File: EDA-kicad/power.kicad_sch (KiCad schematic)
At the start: 99 parts, among them SW6 CHP-041B, U10 BAT-CONNECTOR-FLTS22WR00, U11 BQ25792RQMR, U2 TPS650250RHBR, U3 MP3429GL-Z, U4 TPS650250RHBR

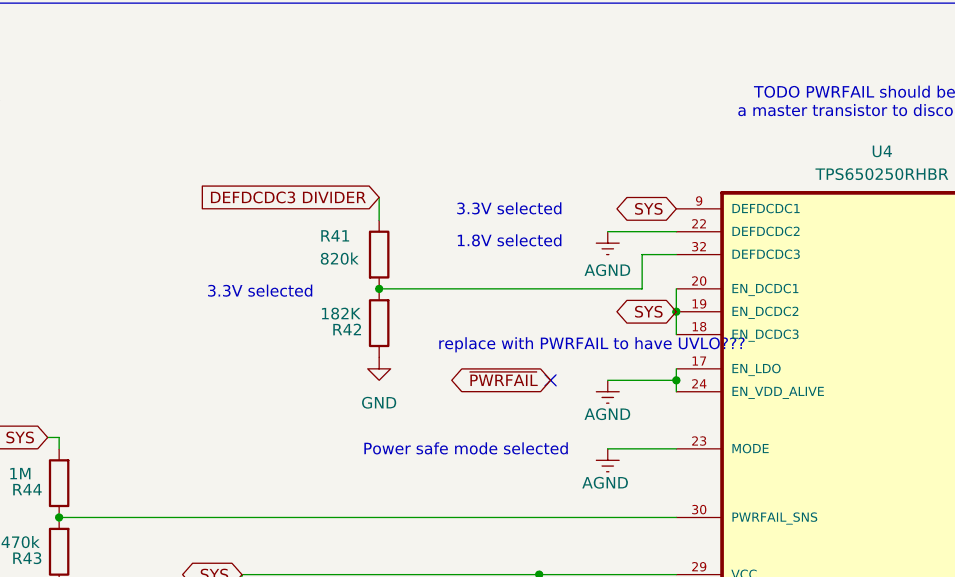
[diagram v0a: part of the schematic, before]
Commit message: separate regulator EN labels for fine grained power saving features etc
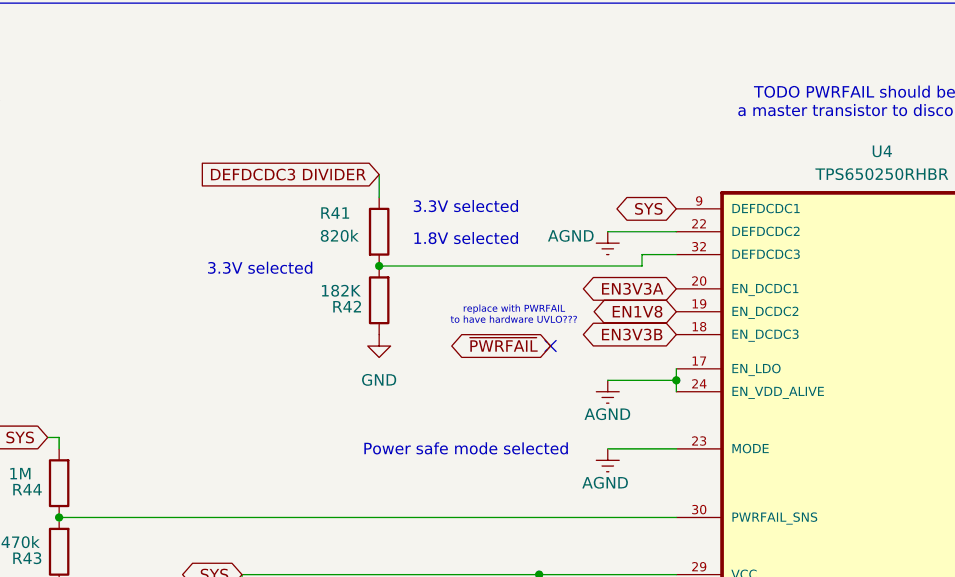
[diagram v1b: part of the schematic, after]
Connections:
- net SYS: no longer U4.18 (EN_DCDC3), U4.19 (EN_DCDC2), U4.20 (EN_DCDC1)
- new net EN1V8: U4.19 (EN_DCDC2)
- new net EN3V3A: U4.20 (EN_DCDC1)
- new net EN3V3B: U4.18 (EN_DCDC3)
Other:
- note added: "replace with PWRFAIL to have hardware UVLO???"
- note removed: "replace with PWRFAIL to have UVLO???"
- moved on the sheet: R41, R42
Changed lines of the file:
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@@
 	(text "1.8V selected"
 		(exclude_from_sim no)
-		(at 321.818 77.47 0)
+		(at 316.992 77.216 0)
 		(effects
 			(font
@@
 		)
 	)
-	(text "replace with PWRFAIL to have UVLO???\n"
+	(text "replace with PWRFAIL\nto have hardware UVLO???\n"
 		(exclude_from_sim no)
-		(at 330.962 88.9 0)
+		(at 322.326 85.598 0)
 		(effects
 			(font
-				(size 1.27 1.27)
+				(size 0.762 0.762)
 			)
 		)
@@
 	(text "3.3V selected"
 		(exclude_from_sim no)
-		(at 294.132 83.058 0)
+		(at 294.132 80.518 0)
 		(effects
 			(font
@@
 	(text "3.3V selected"
 		(exclude_from_sim no)
-		(at 321.818 73.914 0)
+		(at 316.992 73.66 0)
 		(effects
 			(font
@@
 	)
 	(junction
-		(at 307.34 82.55)
+		(at 307.34 80.01)
 		(diameter 0)
 		(color 0 0 0 0)
@@
 	)
 	(junction
-		(at 340.36 85.09)
-		(diameter 0)
-		(color 0 0 0 0)
-	)
-	(junction
 		(at 294.64 121.92)
 		(diameter 0)
@@
 	)
 	(no_connect
-		(at 326.39 92.71)
+		(at 326.39 88.9)
 	)
 	(no_connect
@@
 	(wire
 		(pts
-			(xy 340.36 82.55) (xy 340.36 85.09)
-		)
-		(stroke
-			(width 0)
-			(type default)
-		)
-	)
-	(wire
-		(pts
 			(xy 201.93 205.74) (xy 196.85 205.74)
 		)
@@
 	(wire
 		(pts
-			(xy 340.36 85.09) (xy 340.36 87.63)
-		)
-		(stroke
-			(width 0)
-			(type default)
-		)
-	)
-	(wire
-		(pts
 			(xy 52.07 227.33) (xy 57.15 227.33)
 		)
@@
 	(wire
 		(pts
-			(xy 307.34 82.55) (xy 336.55 82.55)
+			(xy 307.34 80.01) (xy 336.55 80.01)
 		)
 		(stroke
@@
 	(wire
 		(pts
-			(xy 336.55 78.74) (xy 336.55 82.55)
+			(xy 336.55 78.74) (xy 336.55 80.01)
 		)
 		(stroke
@@
 	(wire
 		(pts
-			(xy 307.34 72.39) (xy 307.34 74.93)
+			(xy 307.34 69.85) (xy 307.34 72.39)
 		)
 		(stroke
@@
 		)
 	)
+	(global_label "EN3V3B"
+		(shape bidirectional)
+		(at 340.36 87.63 180)
+		(fields_autoplaced yes)
+		(effects
+			(font
+				(size 1.27 1.27)
+			)
+			(justify right)
+		)
+		(property "Intersheetrefs" "${INTERSHEET_REFS}"
+			(at 329.0064 87.63 0)
+			(effects
+				(font
+					(size 1.27 1.27)
+				)
+				(justify right)
+				(hide yes)
+			)
+		)
+	)
 	(global_label "REGN"
 		(shape bidirectional)
@@
 		)
 	)
+	(global_label "EN1V8"
+		(shape bidirectional)
+		(at 340.36 85.09 180)
+		(fields_autoplaced yes)
+		(effects
+			(font
+				(size 1.27 1.27)
+			)
+			(justify right)
+		)
+		(property "Intersheetrefs" "${INTERSHEET_REFS}"
+			(at 330.2764 85.09 0)
+			(effects
+				(font
+					(size 1.27 1.27)
+				)
+				(justify right)
+				(hide yes)
+			)
+		)
+	)
 	(global_label "VDCDC1"
 		(shape input)
@@
 	(global_label "DEFDCDC3 DIVIDER"
 		(shape input)
-		(at 307.34 72.39 180)
+		(at 307.34 69.85 180)
 		(fields_autoplaced yes)
 		(effects
@@
 		)
 		(property "Intersheetrefs" "${INTERSHEET_REFS}"
-			(at 286.3329 72.39 0)
+			(at 286.3329 69.85 0)
 			(effects
 				(font
@@
 	(global_label "~{PWRFAIL}"
 		(shape bidirectional)
-		(at 326.39 92.71 180)
+		(at 326.39 88.9 180)
 		(fields_autoplaced yes)
 		(effects
@@
 		)
 		(property "Intersheetrefs" "${INTERSHEET_REFS}"
-			(at 314.492 92.71 0)
+			(at 314.492 88.9 0)
 			(effects
 				(font
@@
 		)
 	)
-	(global_label "SYS"
-		(shape bidirectional)
-		(at 340.36 85.09 180)
-		(fields_autoplaced yes)
-		(effects
-			(font
-				(size 1.27 1.27)
-			)
-			(justify right)
-		)
-		(property "Intersheetrefs" "${INTERSHEET_REFS}"
-			(at 332.7559 85.09 0)
-			(effects
-				(font
-					(size 1.27 1.27)
-				)
-				(justify right)
-				(hide yes)
-			)
-		)
-	)
 	(global_label "D+"
 		(shape bidirectional)
@@
 		)
 	)
+	(global_label "EN3V3A"
+		(shape bidirectional)
+		(at 340.36 82.55 180)
+		(fields_autoplaced yes)
+		(effects
+			(font
+				(size 1.27 1.27)
+			)
+			(justify right)
+		)
+		(property "Intersheetrefs" "${INTERSHEET_REFS}"
+			(at 329.1878 82.55 0)
+			(effects
+				(font
+					(size 1.27 1.27)
+				)
+				(justify right)
+				(hide yes)
+			)
+		)
+	)
 	(global_label "1V8"
 		(shape input)
@@
 		)
 		(property "Value" "AGND"
-			(at 332.74 80.518 0)
+			(at 328.676 76.708 0)
 			(effects
 				(font
@@
 	(symbol
 		(lib_id "Device:R")
-		(at 307.34 78.74 0)
+		(at 307.34 76.2 0)
 		(unit 1)
 		(exclude_from_sim no)
@@
 		(dnp no)
 		(property "Reference" "R41"
-			(at 300.736 76.708 0)
+			(at 300.736 74.168 0)
 			(effects
 				(font
@@
 		)
 		(property "Value" "820k"
-			(at 300.736 79.248 0)
+			(at 300.736 76.708 0)
 			(effects
 				(font
@@
 		)
 		(property "Footprint" "SPIRIT-footprints:0603-resistor"
-			(at 305.562 78.74 90)
+			(at 305.562 76.2 90)
 			(effects
 				(font
@@
 		)
 		(property "Datasheet" "~"
-			(at 307.34 78.74 0)
+			(at 307.34 76.2 0)
 			(effects
 				(font
@@
 		)
 		(property "Description" "Resistor"
-			(at 307.34 78.74 0)
+			(at 307.34 76.2 0)
 			(effects
 				(font
@@
 		)
 		(property "MPN" "RC0603JR-07820KL"
-			(at 307.34 78.74 0)
+			(at 307.34 76.2 0)
 			(effects
 				(font
@@
 	(symbol
 		(lib_id "Device:R")
-		(at 307.34 86.36 180)
+		(at 307.34 83.82 180)
 		(unit 1)
 		(exclude_from_sim no)
@@
 		(dnp no)
 		(property "Reference" "R42"
-			(at 303.784 87.122 0)
+			(at 303.784 84.582 0)
 			(effects
 				(font
@@
 		)
 		(property "Value" "182K"
-			(at 303.022 85.344 0)
+			(at 303.022 82.804 0)
 			(effects
 				(font
@@
 		)
 		(property "Footprint" "SPIRIT-footprints:0603-resistor"
-			(at 309.118 86.36 90)
+			(at 309.118 83.82 90)
 			(effects
 				(font
@@
 		)
 		(property "Datasheet" "~"
-			(at 307.34 86.36 0)
+			(at 307.34 83.82 0)
 			(effects
 				(font
@@
 		)
 		(property "Description" "Resistor"
-			(at 307.34 86.36 0)
+			(at 307.34 83.82 0)
 			(effects
 				(font
@@
 		)
 		(property "MPN" "RC0603FR-07182KL"
-			(at 307.34 86.36 90)
+			(at 307.34 83.82 90)
 			(effects
 				(font
@@
 		(lib_name "GND_11")
 		(lib_id "power:GND")
-		(at 307.34 90.17 0)
+		(at 307.34 87.63 0)
 		(unit 1)
 		(exclude_from_sim no)
@@
 		(fields_autoplaced yes)
 		(property "Reference" "#PWR0157"
-			(at 307.34 96.52 0)
+			(at 307.34 93.98 0)
 			(effects
 				(font
@@
 		)
 		(property "Value" "GND"
-			(at 307.34 95.25 0)
+			(at 307.34 92.71 0)
 			(effects
 				(font
@@
 		)
 		(property "Footprint" ""
-			(at 307.34 90.17 0)
+			(at 307.34 87.63 0)
 			(effects
 				(font
@@
 		)
 		(property "Datasheet" ""
-			(at 307.34 90.17 0)
+			(at 307.34 87.63 0)
 			(effects
 				(font
@@
 		)
 		(property "Description" "Power symbol creates a global label with name \"GND\" , ground"
-			(at 307.34 90.17 0)
+			(at 307.34 87.63 0)
 			(effects
 				(font

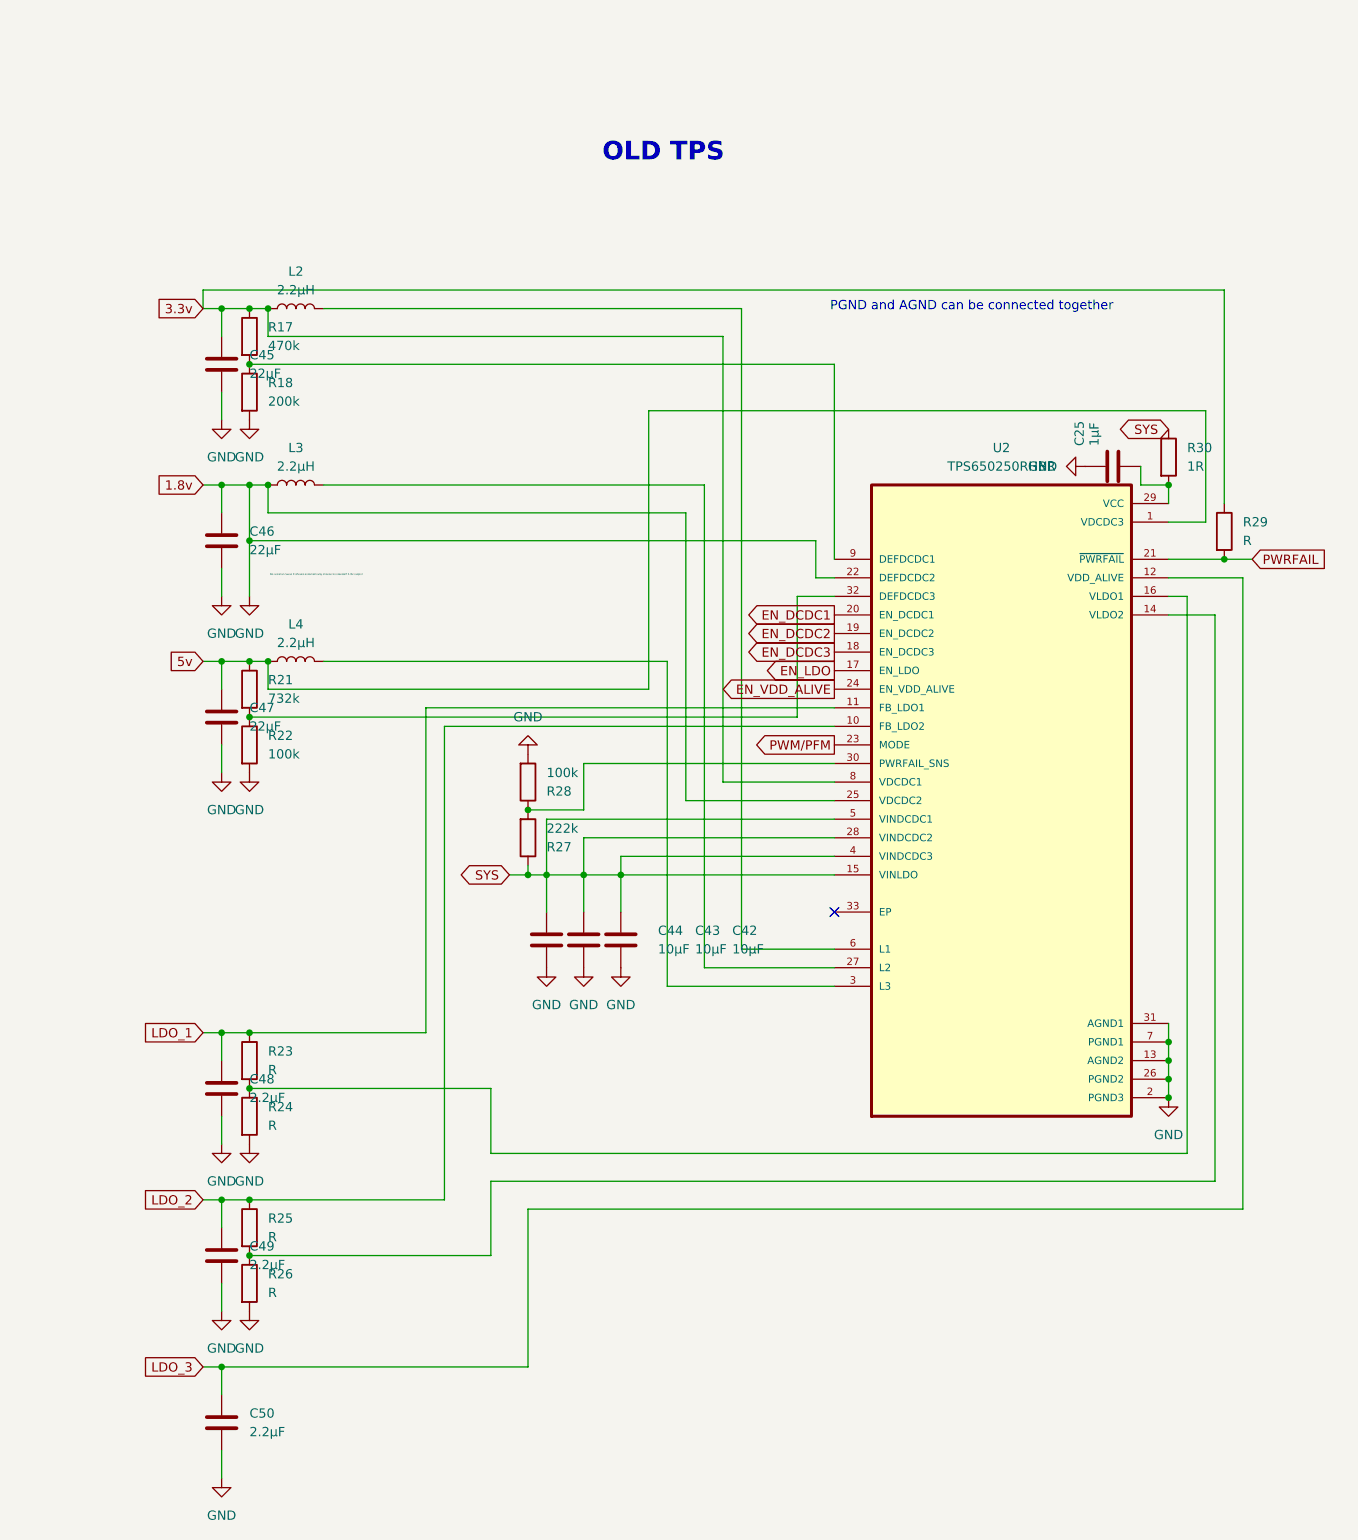
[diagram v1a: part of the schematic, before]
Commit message: remove old TPS650 circuit
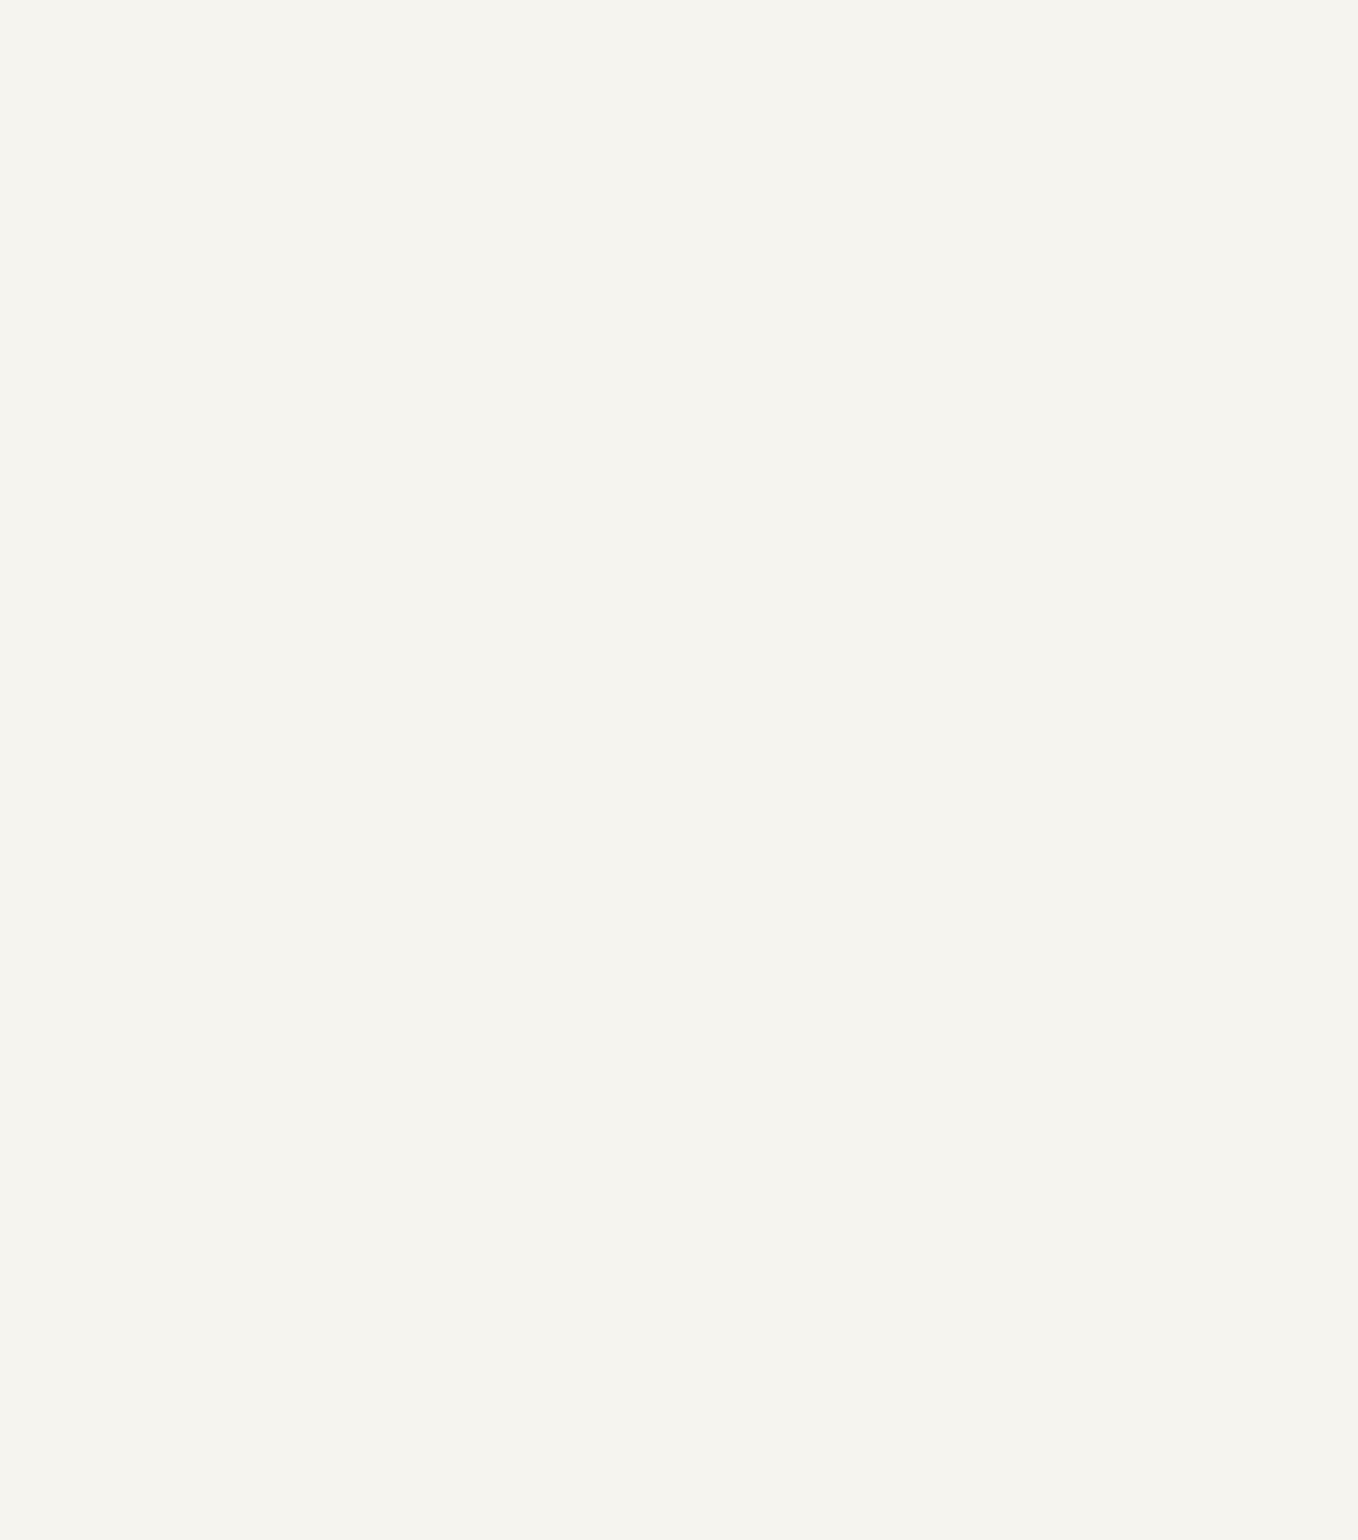
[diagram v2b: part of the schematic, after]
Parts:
- removed C25: 1μF, SPIRIT-footprints:0603-capacitor, symbol Device:C
- removed C42, C43, C44: 10μF, symbol Device:C
- removed C45, C46, C47: 22μF, symbol Device:C
- removed C48, C49, C50: 2.2μF, symbol Device:C
- removed L2, L3, L4: 2.2μH, symbol Device:L
- removed R17: 470k, symbol Device:R
- removed R18: 200k, symbol Device:R
- removed R21: 732k, symbol Device:R
- removed R22, R28: 100k, symbol Device:R
- removed R23, R24, R25, R26, R29: R, symbol Device:R
- removed R27: 222k, symbol Device:R
- removed R30: 1R, symbol Device:R
- removed U2: TPS650250RHBR, TPS650250RHBR:IC_ADS125H01IRHBT, symbol TPS650250RHBR:TPS650250RHBR
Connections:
- no-connect marks 10 -> 9
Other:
- note removed: "No resistor cause it should automatically choose its standart 1.8v output"
- note removed: "OLD TPS"
- note removed: "PGND and AGND can be connected together"

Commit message: add new 22V rail AP3032
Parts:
- added C31, C32: 1μF, SPIRIT-footprints:0603-capacitor, symbol Device:C
- added L6: 6.8μH, symbol Device:L
- added R20: 210k, symbol Device:R
- added R46: 10k, SPIRIT-footprints:0603-resistor, symbol Device:R
- added U2: 22V-boost-AP3032KTR-G1, SPIRIT-footprints:SOT23-6_DIO, symbol SPIRIT-components:22V-boost-AP3032KTR-G1
- R40: value 10k -> 12k; MPN ERA-3AEB103V -> RC0603FR-0712KL
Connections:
- net 22V: now also C31.1, U2.5 (OV)
- net GND: now also C31.2, C32.2, R46.1, U2.2 (GND)
- net LCD_PWM: now also U2.4 (CTRL)
- net SYS: now also C32.1, L6.1, U2.6 (VIN)
- net at R1202N723A-TR-FE1.6 (VFB), R19.2, R31.2: now also R46.2; no longer R40.2
- new net: L6.2, U2.1 (SW)
- new net: R20.2, R40.2, U2.3 (FB)
- no-connect marks 9 -> 10
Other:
- note added: "??????"
- note added: "OLD 22V"
- moved on the sheet: C18, C19, C20, L1, R1202N723A-TR-FE1, R19, R31, R40
